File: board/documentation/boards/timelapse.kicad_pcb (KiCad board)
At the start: 2 copper layers, 49 x 31 mm, 29 parts, among them J1 Battery, J2 OLED-CONN, J3 USB, M1 SMD-XTAL, M2 CAM, Q1 NDS356, SW1 PWR, SW2 PROG, SW3 UP, SW4 DWN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

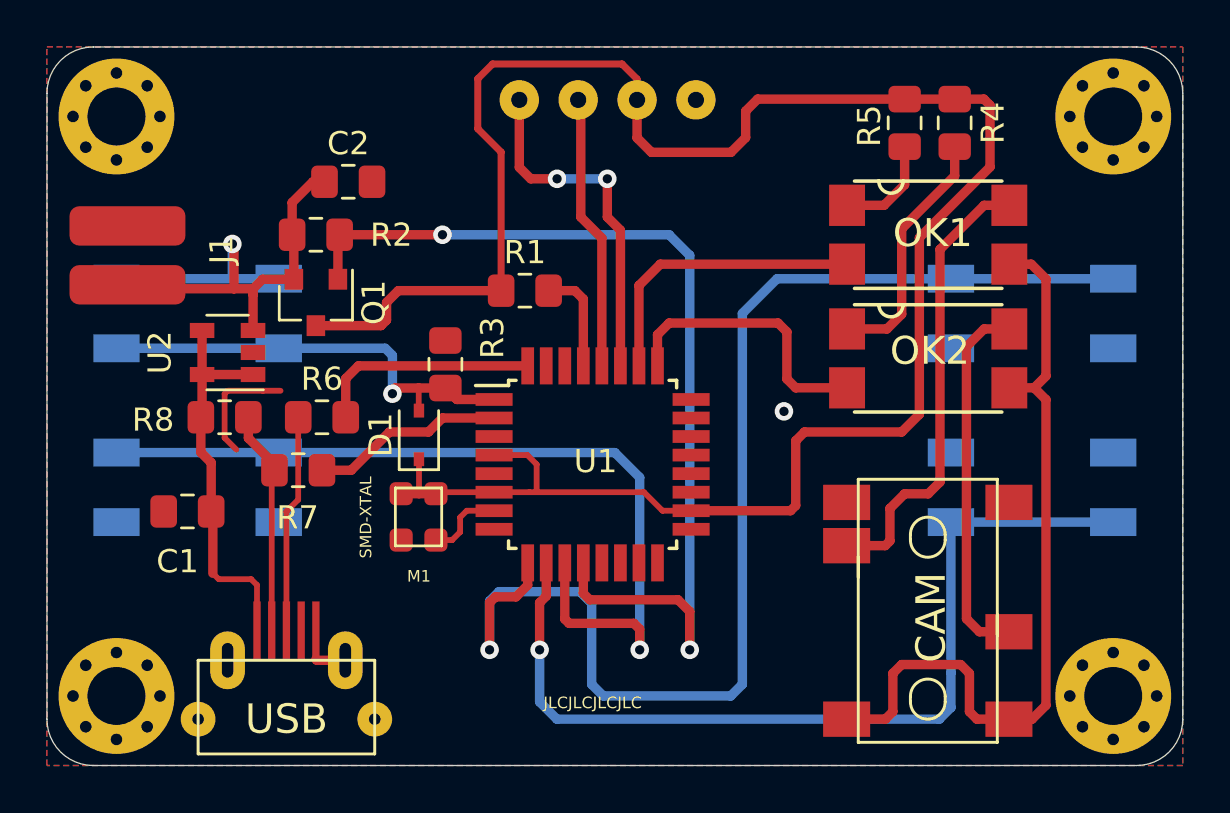
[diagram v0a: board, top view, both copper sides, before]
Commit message: Fixed schematic and board for power control circuit
Power Circuit had problem of leaky IO driver nmos within the controller
added external nmos (2n7002) to take care of proper power on
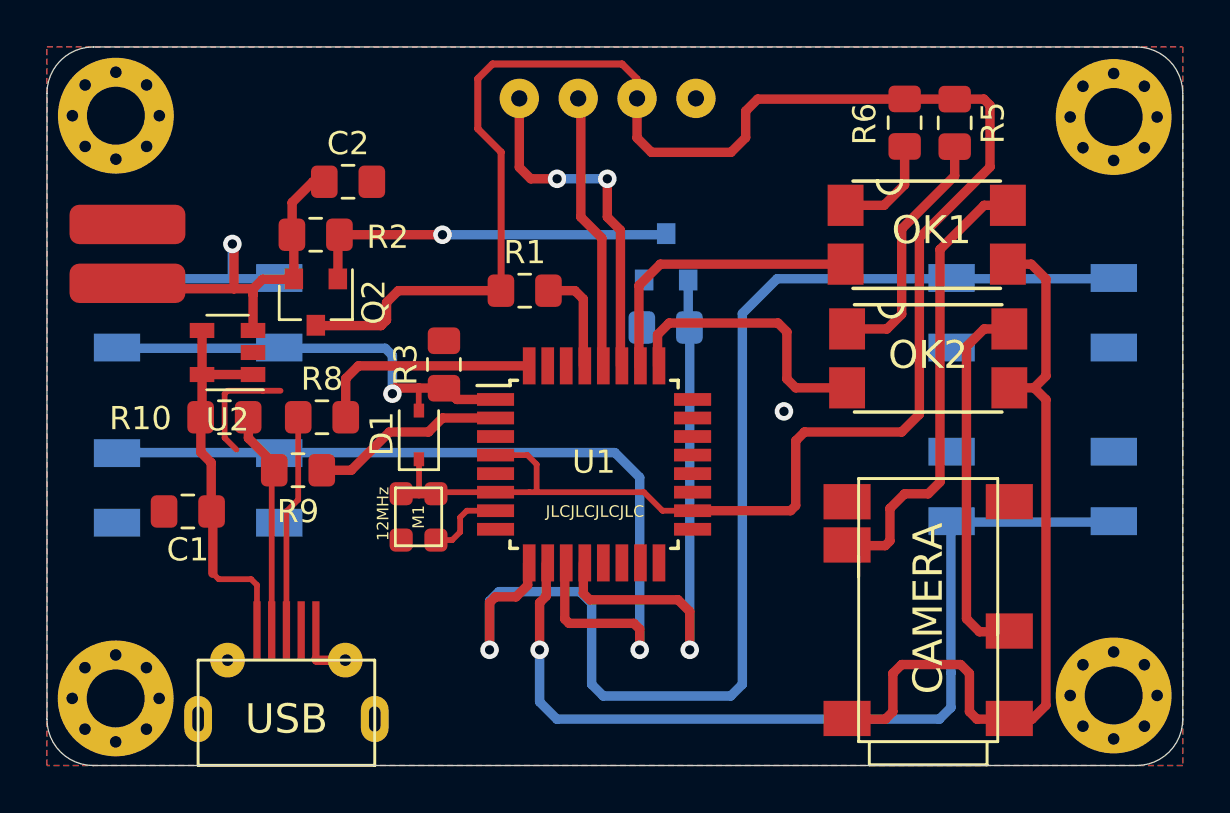
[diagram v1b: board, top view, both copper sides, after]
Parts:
- removed R7: 68, Resistor_SMD:R_0805_2012Metric_Pad1.15x1.40mm_HandSolder
- added Q2: NDS356, Package_TO_SOT_SMD:SOT-23, F.Cu at (117.6, 57.0)
- added R10: 1.5k, Resistor_SMD:R_0805_2012Metric_Pad1.15x1.40mm_HandSolder, F.Cu at (113.7, 62.0)
- added R9: 68, Resistor_SMD:R_0805_2012Metric_Pad1.15x1.40mm_HandSolder, F.Cu at (116.8, 64.3)
- M1: value SMD-XTAL -> 12MHz
- M2: value CAM -> CAMERA
- Q1: value NDS356 -> 2N7002; moved to B.Cu
- R4: value 470 -> 10k; moved to B.Cu
- R6: value 68 -> 470
- R8: value 1.5k -> 68
- moved H3 49.7 mm to (152.0, 74.0)
- moved H1 43.0 mm to (109.0, 49.0), turned to 0 degrees
- moved R6 28.2 mm to (143.0, 49.3), turned to 270 degrees
- moved H2 25.0 mm to (152.0, 49.0)
- moved R4 15.3 mm to (132.7, 58.1), turned to 180 degrees
- moved Q1 15.2 mm to (132.7, 55.1), turned to 90 degrees
- moved R8 4.20 mm to (117.9, 62.0)
- moved R5 2.16 mm to (145.2, 49.3)
- moved H4 0.11 mm to (109.0, 74.1)
- moved R3 0.06 mm to (123.1, 59.7)
- moved J1 0.06 mm to (109.5, 56.2)
- moved J2 0.06 mm to (142.7, 73.5)
- moved OK1 0.06 mm to (144.0, 54.1)
- moved U1 0.06 mm to (129.6, 64.0)
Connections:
- J2 pad 4: LCD_SDA -> Net-(J2-Pad4)
- Q1 pad 2: VBAT -> GND
- Q1 pad 3: VCC -> Net-(Q1-Pad3)
- R2 pad 2: PW_LATCH -> Net-(Q1-Pad3)
- R4 pad 1: VCC -> PW_LATCH
- R4 pad 2: Net-(OK2-Pad1) -> GND
- R5 pad 2: Net-(OK1-Pad1) -> Net-(OK2-Pad1)
- R6 pad 1: Net-(J3-PadD+) -> VCC
- R6 pad 2: USB_DP -> Net-(OK1-Pad1)
- R8 pad 1: VUSB -> Net-(J3-PadD+)
- R8 pad 2: Net-(J3-PadD-) -> USB_DP
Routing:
- net PW_LATCH: track 42.3 -> 23.9 mm, vias 2 -> 1
- net Net-(Q1-Pad3): track 0.00 -> 16.2 mm, vias 0 -> 1
